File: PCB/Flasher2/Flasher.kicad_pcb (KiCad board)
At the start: 2 copper layers, 70 x 70 mm, 62 parts, among them J1 Reset, J2 RJ12, J3 USB, J4 USB-C-Socket-V, J5 TF_PUSH, SW1 SW_Push_DPDT, U1 ESP32-S3-MINI-1-N4R2, U2 TPS562246, U3 FT231XQ, U4 TPS22916CNYFPR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

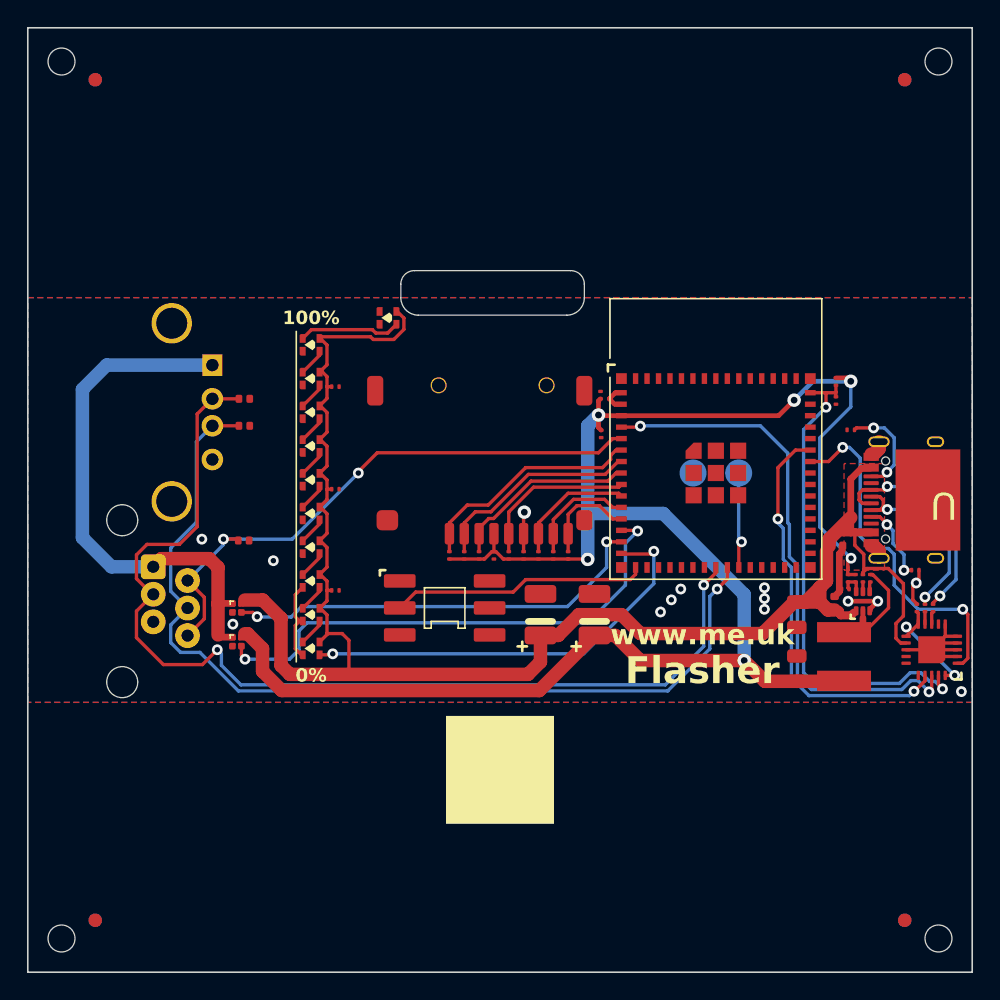
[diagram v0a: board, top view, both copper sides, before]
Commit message: Started Flasher 2 layout
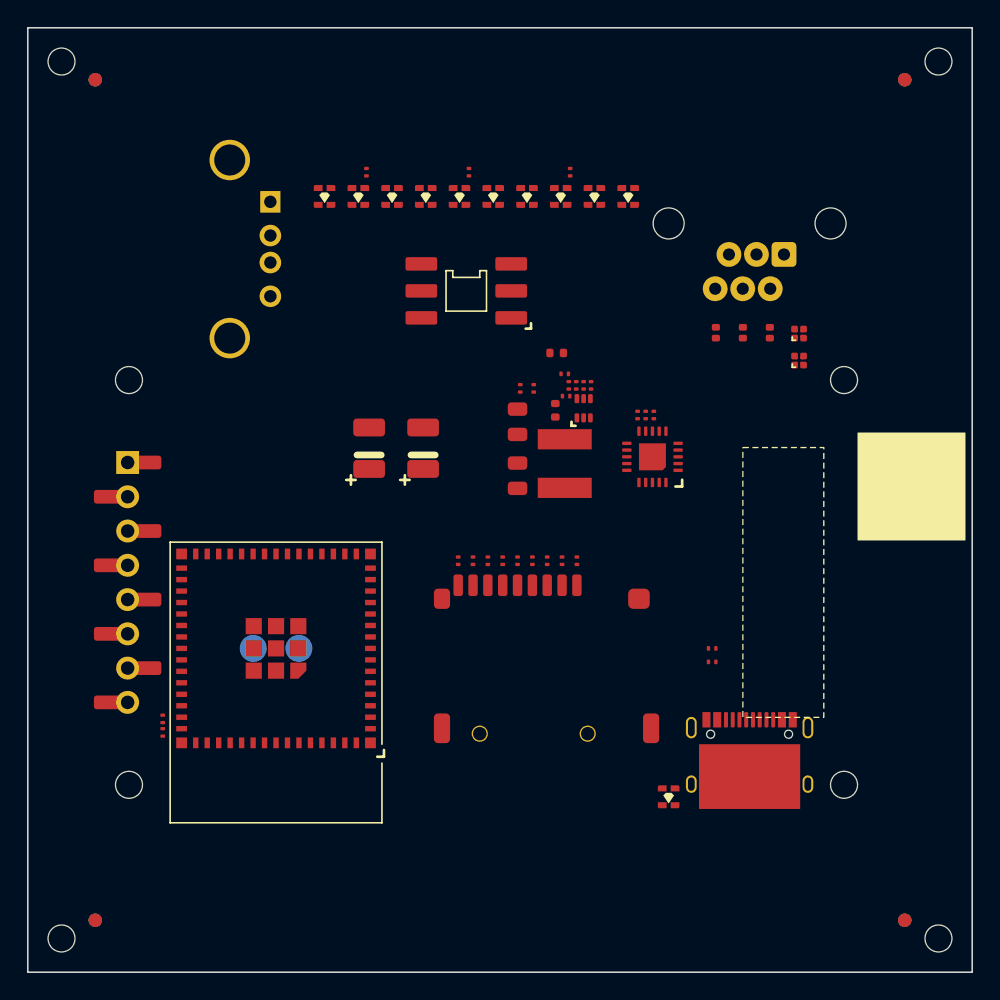
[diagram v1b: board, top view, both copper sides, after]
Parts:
- added J6: LCD, RevK:LCD2, F.Cu at (134.0, 71.1)
- U1: value ESP32-S3-MINI-1-N4R2 -> ESP32-S3-MINI-1
- moved R2 55.8 mm to (110.0, 81.2)
- moved C4 55.6 mm to (110.0, 82.2)
- moved J2 54.3 mm to (153.5, 44.5), turned to 180 degrees
- moved U5 46.6 mm to (157.2, 54.7), turned to -90 degrees
- moved U4 46.4 mm to (157.2, 52.7), turned to -90 degrees
- moved D11 41.1 mm to (147.5, 87.0), turned to 90 degrees
- moved D1 40.9 mm to (144.5, 42.5), turned to 90 degrees
- moved D12 39.3 mm to (155.0, 52.6), turned to 90 degrees
- moved D14 38.2 mm to (151.0, 52.6), turned to -90 degrees
- moved D13 37.6 mm to (153.0, 52.6), turned to 90 degrees
- moved D2 37.4 mm to (142.0, 42.5), turned to 90 degrees
- moved C16 35.5 mm to (140.2, 40.7), turned to 90 degrees
- moved J1 35.1 mm to (118.4, 76.0)
- moved U1 35.1 mm to (118.4, 76.0), turned to 180 degrees
- moved D3 34.0 mm to (139.5, 42.5), turned to 90 degrees
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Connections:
- net LED renamed LEDO
- D11 pad 4: unconnected-(D11-O-Pad4) -> LEDI
- U1 pad 17: unconnected-(U1-GPIO13-Pad17) -> LEDI
- U1 pad 33: unconnected-(U1-GPIO37-Pad33) -> DIN
- U1 pad 34: unconnected-(U1-GPIO38-Pad34) -> CLK
- U1 pad 35: unconnected-(U1-GPIO39-Pad35) -> CS
- U1 pad 36: unconnected-(U1-GPIO40-Pad36) -> DC
- U1 pad 37: unconnected-(U1-GPIO41-Pad37) -> RST
- U1 pad 38: unconnected-(U1-GPIO42-Pad38) -> BL
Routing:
- net +3.3V: track 132.9 -> 0.00 mm, vias 6 -> 0
- net VBUS: track 125.5 -> 0.00 mm
- net D-: track 76.7 -> 0.00 mm, vias 2 -> 0
- net D+: track 69.7 -> 0.00 mm, vias 1 -> 0
- net LOOP: track 42.8 -> 0.00 mm, vias 2 -> 0
- net GPIO0: track 42.1 -> 0.00 mm, vias 2 -> 0
- net VOUT: track 40.0 -> 0.00 mm
- net PWR3: track 38.0 -> 0.00 mm, vias 2 -> 0
- net RST: track 36.9 -> 0.00 mm, vias 2 -> 0
- net GND: track 33.4 -> 0.00 mm, vias 14 -> 0
- net LEDO: track 31.8 -> 0.00 mm, vias 2 -> 0
- net PWR5: track 31.7 -> 0.00 mm, vias 2 -> 0
- net RXD: track 30.2 -> 0.00 mm, vias 2 -> 0
- net TXD: track 26.2 -> 0.00 mm, vias 2 -> 0
- net BTN: track 19.0 -> 0.00 mm
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- removed copper zone on B.Cu, net GND
- removed copper zone on F.Cu, net GND
- removed copper zone on F.Cu, net VBUS
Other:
- board text removed: "+"
- board text removed: "-"
- board text removed: "0%"
- board text removed: "1"
- board text removed: "100%"
- board text removed: "12"
- board text removed: "19"
- board text removed: "2 3 4 5 6 7 8"
- board text removed: "20"
- board text removed: "21"
- board text removed: "9 10 11"
- board text removed: "A"
- board text removed: "DAT2 DAT3 CMD CLK DAT0 DAT1 CD"
- board text removed: "Flasher"
- board text removed: "Made in China for Andrews&Arnold Ltd ${CURRENT_DATE} Code flasher"
- board text removed: "PWR3 PWR5 LED"
- board text removed: "TC2030"
- board text removed: "U"
- board text removed: "www.me.uk"

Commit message: Library update
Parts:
- removed SW1: SW_Push_DPDT, RevK:SW_Push_DPDT
- added SW3: SW_Push_SPDT, RevK:PS-12E15, F.Cu at (154.0, 49.0)
- moved D10 38.0 mm to (160.0, 42.0), turned to -90 degrees
- moved D9 33.0 mm to (157.5, 42.0), turned to -90 degrees
- moved C14 32.0 mm to (156.9, 43.8), turned to -90 degrees
- moved D8 28.0 mm to (155.0, 42.0), turned to -90 degrees
- moved D12 26.0 mm to (129.0, 52.7)
- moved D13 26.0 mm to (127.0, 52.7)
- moved D14 26.0 mm to (125.0, 52.7)
- moved U4 26.0 mm to (131.2, 52.8)
- moved U5 26.0 mm to (131.2, 54.8)
- moved J2 26.0 mm to (127.5, 44.5)
- moved D7 23.0 mm to (152.5, 42.0), turned to -90 degrees
- moved D6 18.0 mm to (150.0, 42.0), turned to -90 degrees
- moved C15 16.9 mm to (149.3, 43.8), turned to -90 degrees
- moved D5 13.0 mm to (147.5, 42.0), turned to -90 degrees
- moved D4 8.02 mm to (145.0, 42.0), turned to -90 degrees
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
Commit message: Library update
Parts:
- U2: footprint RevK:SOT-563 -> RevK:SOT-5x3-6
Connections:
- SW3 pad 1: (no net) -> unconnected-(SW3-A-Pad1)
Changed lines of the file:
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@@
 	(net 69 "LEDO")
 	(net 70 "LEDI")
+	(net 71 "unconnected-(SW3-A-Pad1)")
 	(footprint "RevK:USB-C-Socket-H"
 		(layer "F.Cu")
@@
 		)
 	)
-	(footprint "RevK:SOT-563"
+	(footprint "RevK:SOT-5x3-6"
 		(layer "F.Cu")
 		(at 141.2 58.2 90)
@@
 		(sheetname "/")
 		(sheetfile "Flasher.kicad_sch")
+		(zone_connect 2)
 		(attr smd)
 		(fp_line
@@
 			)
 		)
-		(property "MPN" "C2848950"
+		(property "MPN" "C2848946"
 			(at 0 0 0)
 			(unlocked yes)
@@
 			(layers "*.Cu" "*.Mask")
 			(remove_unused_layers no)
+			(net 71 "unconnected-(SW3-A-Pad1)")
+			(pinfunction "A")
+			(pintype "passive+no_connect")
 		)
 		(pad "2" thru_hole circle
@@
 			(remove_unused_layers no)
 			(net 1 "GND")
-			(pinfunction "A")
+			(pinfunction "C")
 			(pintype "passive")
 		)

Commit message: Library update
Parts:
- D11: footprint RevK:SMD1615 -> RevK:SMD1615-Side
- moved R8 10.8 mm to (158.5, 84.5), turned to 90 degrees
- moved R7 8.79 mm to (148.5, 84.5), turned to -90 degrees
- moved C2 8.28 mm to (137.5, 46.0)
- moved C35 7.84 mm to (121.5, 62.0)
- moved C17 7.84 mm to (117.5, 62.0)
- moved U5 3.87 mm to (134.5, 52.8), turned to 180 degrees
- moved C1 3.80 mm to (132.5, 59.2)
- moved C10 3.80 mm to (132.7, 56.7)
- moved C5 3.80 mm to (137.9, 56.5)
- moved C7 3.80 mm to (132.5, 63.2)
- moved C8 3.80 mm to (133.7, 56.7), turned to 90 degrees
- moved C9 3.80 mm to (136.0, 55.6)
- moved L1 3.80 mm to (136.0, 62.3)
- moved R3 3.80 mm to (136.8, 56.5)
- moved R4 3.80 mm to (136.1, 57.3)
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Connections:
- C4 pad 1: RST -> RESET
- R2 pad 2: RST -> RESET
- U1 pad 45: RST -> RESET
- U3 pad 19: RST -> RESET
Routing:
- net VBUS: track 0.00 -> 150.3 mm, vias 0 -> 4
- net +3.3V: track 0.00 -> 126.6 mm, vias 0 -> 5
- net RESET: track 0.00 -> 65.0 mm, vias 0 -> 2
- net Net-(D10-O): track 0.00 -> 60.3 mm, vias 0 -> 2
- net RXD: track 0.00 -> 55.7 mm, vias 0 -> 2
- net GND: track 0.00 -> 54.4 mm, vias 0 -> 23
- net TXD: track 0.00 -> 53.9 mm, vias 0 -> 2
- net D-: track 0.00 -> 46.5 mm, vias 0 -> 1
- net D+: track 0.00 -> 43.7 mm, vias 0 -> 1
- net BTN: track 0.00 -> 42.5 mm, vias 0 -> 1
- net LEDI: track 0.00 -> 42.5 mm, vias 0 -> 2
- net LOOP: track 0.00 -> 39.4 mm, vias 0 -> 1
- net PWR3: track 0.00 -> 36.1 mm, vias 0 -> 2
- net LEDO: track 0.00 -> 32.8 mm, vias 0 -> 2
- net Net-(J4-D+-PadA6): track 0.00 -> 32.7 mm, vias 0 -> 2
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- added copper zone on B.Cu, net GND
- added copper zone on F.Cu, net GND
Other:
- board text added: "0 1 2 3 4 5 6 7 8 9 10 11 12 13 37 38 39 40 41 42 43 44"
- board text added: "5V"
- board text added: "A"
- board text added: "BOOT LOOP SDDAT2 SDDAT3 SDCMD SDCLK SDDAT0 SDDAT1 SDCD PWR3 PWR5 LEDO BTN LEDI DIN CLK CS DC RST BL TXD RXD"
- board text added: "Flasher"
- board text added: "Flasher ${CURRENT_DATE}"
- board text added: "Made in China for Andrews & Arnold Ltd"
- board text added: "TC2030"
- board text added: "U"

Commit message: Library update
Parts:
- moved C2 24.1 mm to (161.5, 44.0)
- moved C9 1.64 mm to (134.4, 56.2), turned to -90 degrees
- moved U5 0.73 mm to (135.1, 52.4)
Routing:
- net GND: track 54.4 -> 50.9 mm, vias 23 -> 28
- net +3.3V: track 126.6 -> 125.4 mm
- net PWR3: track 36.1 -> 35.0 mm
- net Net-(U3-3V3OUT): track 13.3 -> 14.1 mm
- net VOUT: track 22.6 -> 23.3 mm
- net VBUS: track 150.3 -> 149.7 mm
- net BTN: track 42.5 -> 41.9 mm
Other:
- board text added: "5V DC"
- board text removed: "5V"

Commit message: Library update
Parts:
- moved D11 3.04 mm to (144.0, 87.5)
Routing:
- net Net-(D10-O): track 60.2 -> 65.9 mm
- net LEDI: track 42.5 -> 39.4 mm
- net VBUS: track 149.7 -> 152.2 mm

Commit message: As ordered
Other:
- board text added: "1 2 3 4 5 6 7 8 9 10 11 12 13 37 38 39 40 41 42 43 44"
- board text added: "ESP32 TC2030 Code Flasher ${CURRENT_DATE}"
- board text added: "LOOP SDDAT2 SDDAT3 SDCMD SDCLK SDDAT0 SDDAT1 SDCD PWR3 PWR5 LEDO BTN LEDI DIN CLK CS DC RST BL TXD RXD"
- board text removed: "0 1 2 3 4 5 6 7 8 9 10 11 12 13 37 38 39 40 41 42 43 44"
- board text removed: "BOOT LOOP SDDAT2 SDDAT3 SDCMD SDCLK SDDAT0 SDDAT1 SDCD PWR3 PWR5 LEDO BTN LEDI DIN CLK CS DC RST BL TXD RXD"
- board text removed: "Flasher ${CURRENT_DATE}"

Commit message: Library update
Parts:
- moved C2 23.1 mm to (142.4, 57.0)
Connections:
- C14 pad 1: VBUS -> +3.3V
- C15 pad 1: VBUS -> +3.3V
- C16 pad 1: VBUS -> +3.3V
- D1 pad 3: VBUS -> +3.3V
- D10 pad 3: VBUS -> +3.3V
- D11 pad 3: VBUS -> +3.3V
- D2 pad 3: VBUS -> +3.3V
- D3 pad 3: VBUS -> +3.3V
- D4 pad 3: VBUS -> +3.3V
- D5 pad 3: VBUS -> +3.3V
- D6 pad 3: VBUS -> +3.3V
- D7 pad 3: VBUS -> +3.3V
- D8 pad 3: VBUS -> +3.3V
- D9 pad 3: VBUS -> +3.3V
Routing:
- net VBUS: track 152.2 -> 97.2 mm
- net +3.3V: track 125.4 -> 174.1 mm
- net GND: track 50.9 -> 57.4 mm
- net PWR3: track 35.0 -> 35.9 mm
